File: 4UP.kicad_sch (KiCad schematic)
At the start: 34 parts, among them CON1 BARREL_JACK, J1 Conn_01x02_Male, J2 Conn_01x02_Male, J3 Conn_01x02_Male, P1 CONN_02X08, P2 CONN_02X08, SW1 SW_SPST, U1 VX078012-1000, U2 VX078012-1000, U3 VX078-500

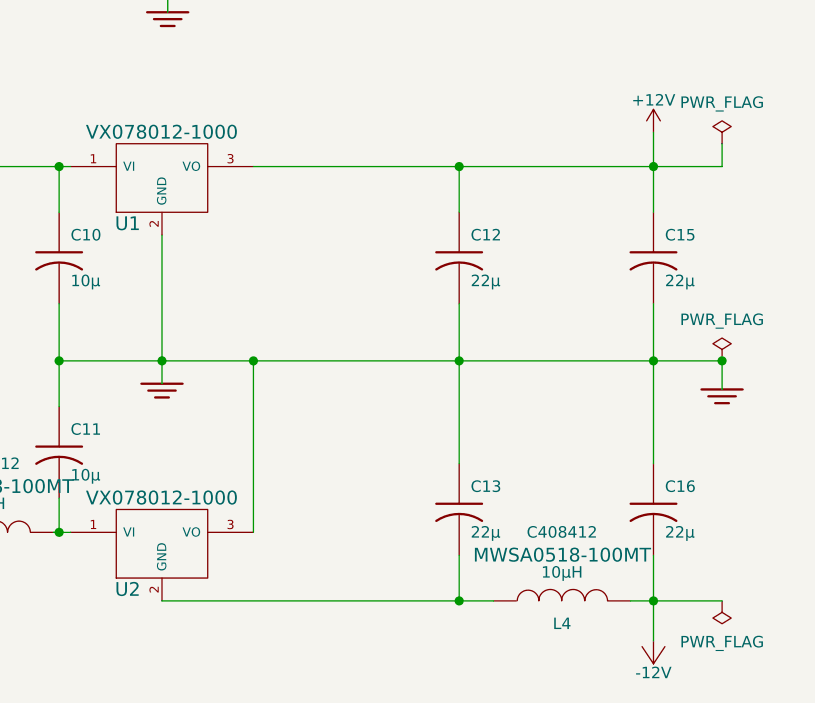
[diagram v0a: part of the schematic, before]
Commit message: fixed interference between bulk caps and VXO PSUs
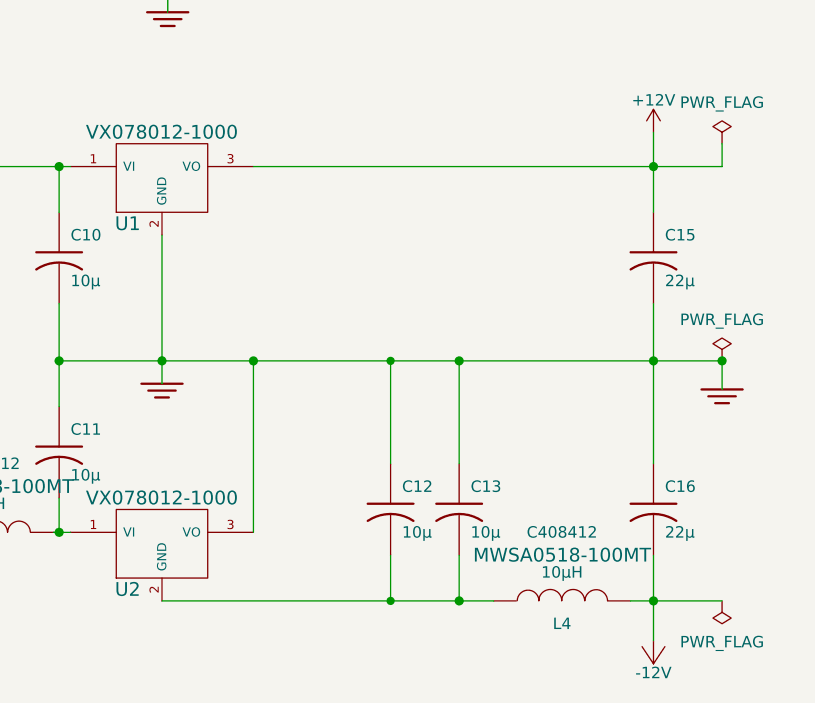
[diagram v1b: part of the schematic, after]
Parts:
- C12, C13: value 22µ -> 10µ; footprint Capacitor_SMD:C_1206_3216Metric -> Capacitor_SMD:C_0603_1608Metric; LCSC C12891 -> C96446
- L1, L2, L3, L4: footprint Inductor_SMD:L_Sunlord_MWSA0518_5.4x5.2mm -> MyFootprints:L_Sunlord_MWSA0518_5.4x5.2mm
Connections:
- net +12V: no longer C12.1
- net GND: now also C12.1; no longer C12.2
- net at C13.2, L4.1, U2.2 (GND): now also C12.2
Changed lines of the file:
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@@
   (junction (at 486.41 321.945) (diameter 1.016) (color 0 0 0 0)
   )
+  (junction (at 478.79 321.945) (diameter 0) (color 0 0 0 0)
+  )
   (junction (at 473.71 178.435) (diameter 0) (color 0 0 0 0)
   )
@@
   (junction (at 334.645 229.235) (diameter 1.016) (color 0 0 0 0)
   )
+  (junction (at 478.79 348.615) (diameter 0) (color 0 0 0 0)
+  )
   (junction (at 497.84 133.985) (diameter 1.016) (color 0 0 0 0)
   )
@@
   )
   (junction (at 453.39 321.945) (diameter 1.016) (color 0 0 0 0)
-  )
-  (junction (at 486.41 300.355) (diameter 1.016) (color 0 0 0 0)
   )
   (junction (at 515.62 321.945) (diameter 1.016) (color 0 0 0 0)
@@
     (stroke (width 0) (type solid) (color 0 0 0 0))
   )
-  (wire (pts (xy 453.39 348.615) (xy 486.41 348.615))
+  (wire (pts (xy 453.39 348.615) (xy 478.79 348.615))
     (stroke (width 0) (type solid) (color 0 0 0 0))
   )
@@
     (stroke (width 0) (type solid) (color 0 0 0 0))
   )
+  (wire (pts (xy 478.79 343.535) (xy 478.79 348.615))
+    (stroke (width 0) (type default) (color 0 0 0 0))
+  )
   (wire (pts (xy 487.045 280.035) (xy 487.045 278.765))
     (stroke (width 0) (type solid) (color 0 0 0 0))
@@
     (stroke (width 0) (type solid) (color 0 0 0 0))
   )
-  (wire (pts (xy 463.55 321.945) (xy 486.41 321.945))
+  (wire (pts (xy 463.55 321.945) (xy 478.79 321.945))
     (stroke (width 0) (type solid) (color 0 0 0 0))
   )
@@
     (stroke (width 0) (type solid) (color 0 0 0 0))
   )
-  (wire (pts (xy 486.41 315.595) (xy 486.41 321.945))
-    (stroke (width 0) (type solid) (color 0 0 0 0))
-  )
   (wire (pts (xy 486.41 321.945) (xy 486.41 333.375))
     (stroke (width 0) (type solid) (color 0 0 0 0))
@@
     (stroke (width 0) (type solid) (color 0 0 0 0))
   )
+  (wire (pts (xy 478.79 321.945) (xy 486.41 321.945))
+    (stroke (width 0) (type solid) (color 0 0 0 0))
+  )
   (wire (pts (xy 458.47 128.905) (xy 449.58 128.905))
     (stroke (width 0) (type solid) (color 0 0 0 0))
@@
   (wire (pts (xy 422.275 300.355) (xy 441.96 300.355))
     (stroke (width 0) (type solid) (color 0 0 0 0))
+  )
+  (wire (pts (xy 478.79 321.945) (xy 478.79 333.375))
+    (stroke (width 0) (type default) (color 0 0 0 0))
   )
   (wire (pts (xy 422.275 300.355) (xy 422.275 340.995))
@@
     (stroke (width 0) (type solid) (color 0 0 0 0))
   )
-  (wire (pts (xy 486.41 300.355) (xy 508 300.355))
+  (wire (pts (xy 463.55 300.355) (xy 508 300.355))
     (stroke (width 0) (type solid) (color 0 0 0 0))
   )
@@
     (stroke (width 0) (type solid) (color 0 0 0 0))
   )
+  (wire (pts (xy 478.79 348.615) (xy 486.41 348.615))
+    (stroke (width 0) (type solid) (color 0 0 0 0))
+  )
   (wire (pts (xy 400.685 265.43) (xy 400.685 300.355))
     (stroke (width 0) (type solid) (color 0 0 0 0))
@@
     (stroke (width 0) (type solid) (color 0 0 0 0))
   )
-  (wire (pts (xy 486.41 300.355) (xy 486.41 305.435))
-    (stroke (width 0) (type solid) (color 0 0 0 0))
-  )
   (wire (pts (xy 405.765 265.43) (xy 400.685 265.43))
     (stroke (width 0) (type solid) (color 0 0 0 0))
@@
     (stroke (width 0) (type solid) (color 0 0 0 0))
   )
-  (wire (pts (xy 463.55 300.355) (xy 486.41 300.355))
-    (stroke (width 0) (type solid) (color 0 0 0 0))
-  )
   (wire (pts (xy 340.36 236.22) (xy 340.36 229.235))
     (stroke (width 0) (type solid) (color 0 0 0 0))
@@
     (pin "~")
   )
-  (symbol (lib_id "VXO_PSU-rescue:C_US") (at 486.41 310.515 0) (unit 1)
-    (in_bom yes) (on_board yes)
-    (property "Reference" "C12" (id 0) (at 487.68 307.975 0)
-      (effects (font (size 1.27 1.27)) (justify left))
-    )
-    (property "Value" "22µ" (id 1) (at 487.68 313.055 0)
-      (effects (font (size 1.27 1.27)) (justify left))
-    )
-    (property "Footprint" "Capacitor_SMD:C_1206_3216Metric" (id 2) (at 486.41 310.515 0)
-      (effects (font (size 1.524 1.524)) hide)
-    )
-    (property "Datasheet" "" (id 3) (at 486.41 310.515 0)
-      (effects (font (size 1.524 1.524)))
-    )
-    (property "LCSC" "C12891" (id 4) (at 486.41 310.515 0)
-      (effects (font (size 1.27 1.27)) hide)
-    )
-    (pin "1")
-    (pin "2")
-  )
   (symbol (lib_id "VXO_PSU-rescue:C_US") (at 441.96 310.515 0) (unit 1)
     (in_bom yes) (on_board yes)
@@
     (property "Reference" "L1" (id 0) (at 412.75 302.895 90))
     (property "Value" "10µH" (id 1) (at 412.75 297.18 90))
-    (property "Footprint" "Inductor_SMD:L_Sunlord_MWSA0518_5.4x5.2mm" (id 2) (at 412.75 300.355 0)
+    (property "Footprint" "MyFootprints:L_Sunlord_MWSA0518_5.4x5.2mm" (id 2) (at 412.75 300.355 0)
       (effects (font (size 1.524 1.524)) hide)
     )
@@
       (effects (font (size 1.27 1.27)) (justify left))
     )
-    (property "Value" "22µ" (id 1) (at 487.68 340.995 0)
-      (effects (font (size 1.27 1.27)) (justify left))
-    )
-    (property "Footprint" "Capacitor_SMD:C_1206_3216Metric" (id 2) (at 486.41 338.455 0)
+    (property "Value" "10µ" (id 1) (at 487.68 340.995 0)
+      (effects (font (size 1.27 1.27)) (justify left))
+    )
+    (property "Footprint" "Capacitor_SMD:C_0603_1608Metric" (id 2) (at 486.41 338.455 0)
       (effects (font (size 1.524 1.524)) hide)
     )
@@
       (effects (font (size 1.524 1.524)))
     )
-    (property "LCSC" "C12891" (id 4) (at 486.41 338.455 0)
+    (property "LCSC" "C96446" (id 4) (at 486.41 338.455 0)
       (effects (font (size 1.27 1.27)) hide)
     )
@@
     (property "Reference" "L3" (id 0) (at 433.705 343.535 90))
     (property "Value" "10µH" (id 1) (at 433.705 337.82 90))
-    (property "Footprint" "Inductor_SMD:L_Sunlord_MWSA0518_5.4x5.2mm" (id 2) (at 433.705 340.995 0)
+    (property "Footprint" "MyFootprints:L_Sunlord_MWSA0518_5.4x5.2mm" (id 2) (at 433.705 340.995 0)
       (effects (font (size 1.524 1.524)) hide)
     )
@@
     (property "Reference" "L4" (id 0) (at 497.84 351.155 90))
     (property "Value" "10µH" (id 1) (at 497.84 345.44 90))
-    (property "Footprint" "Inductor_SMD:L_Sunlord_MWSA0518_5.4x5.2mm" (id 2) (at 497.84 348.615 0)
+    (property "Footprint" "MyFootprints:L_Sunlord_MWSA0518_5.4x5.2mm" (id 2) (at 497.84 348.615 0)
       (effects (font (size 1.524 1.524)) hide)
     )
@@
     )
     (pin "~")
+  )
+  (symbol (lib_id "VXO_PSU-rescue:C_US") (at 478.79 338.455 0) (unit 1)
+    (in_bom yes) (on_board yes)
+    (property "Reference" "C12" (id 0) (at 480.06 335.915 0)
+      (effects (font (size 1.27 1.27)) (justify left))
+    )
+    (property "Value" "10µ" (id 1) (at 480.06 340.995 0)
+      (effects (font (size 1.27 1.27)) (justify left))
+    )
+    (property "Footprint" "Capacitor_SMD:C_0603_1608Metric" (id 2) (at 478.79 338.455 0)
+      (effects (font (size 1.524 1.524)) hide)
+    )
+    (property "Datasheet" "" (id 3) (at 478.79 338.455 0)
+      (effects (font (size 1.524 1.524)))
+    )
+    (property "LCSC" "C96446" (id 4) (at 478.79 338.455 0)
+      (effects (font (size 1.27 1.27)) hide)
+    )
+    (pin "1")
+    (pin "2")
   )
   (symbol (lib_id "power1:+12V") (at 340.36 217.805 0) (unit 1)
@@
     (property "Reference" "L2" (id 0) (at 413.385 267.97 90))
     (property "Value" "10µH" (id 1) (at 413.385 262.255 90))
-    (property "Footprint" "Inductor_SMD:L_Sunlord_MWSA0518_5.4x5.2mm" (id 2) (at 413.385 265.43 0)
+    (property "Footprint" "MyFootprints:L_Sunlord_MWSA0518_5.4x5.2mm" (id 2) (at 413.385 265.43 0)
       (effects (font (size 1.524 1.524)) hide)
     )
@@
       (reference "C11") (unit 1) (value "10µ") (footprint "Capacitor_SMD:C_1206_3216Metric")
     )
-    (path "/00000000-0000-0000-0000-00005c480515"
-      (reference "C12") (unit 1) (value "22µ") (footprint "Capacitor_SMD:C_1206_3216Metric")
+    (path "/8dca1a50-0e75-490e-b512-fa5cf96dc6c4"
+      (reference "C12") (unit 1) (value "10µ") (footprint "Capacitor_SMD:C_0603_1608Metric")
     )
     (path "/00000000-0000-0000-0000-00005c4bf97a"
-      (reference "C13") (unit 1) (value "22µ") (footprint "Capacitor_SMD:C_1206_3216Metric")
+      (reference "C13") (unit 1) (value "10µ") (footprint "Capacitor_SMD:C_0603_1608Metric")
     )
     (path "/00000000-0000-0000-0000-00005d9b97e5"
@@
     )
     (path "/00000000-0000-0000-0000-00005c480569"
-      (reference "L1") (unit 1) (value "10µH") (footprint "Inductor_SMD:L_Sunlord_MWSA0518_5.4x5.2mm")
+      (reference "L1") (unit 1) (value "10µH") (footprint "MyFootprints:L_Sunlord_MWSA0518_5.4x5.2mm")
     )
     (path "/fff1db2b-1e63-4b1a-a271-5f15da541abd"
-      (reference "L2") (unit 1) (value "10µH") (footprint "Inductor_SMD:L_Sunlord_MWSA0518_5.4x5.2mm")
+      (reference "L2") (unit 1) (value "10µH") (footprint "MyFootprints:L_Sunlord_MWSA0518_5.4x5.2mm")
     )
     (path "/6383d9be-0754-4e78-b20d-99bb0b069c96"
-      (reference "L3") (unit 1) (value "10µH") (footprint "Inductor_SMD:L_Sunlord_MWSA0518_5.4x5.2mm")
+      (reference "L3") (unit 1) (value "10µH") (footprint "MyFootprints:L_Sunlord_MWSA0518_5.4x5.2mm")
     )
     (path "/697b9523-6938-475e-b51c-ef53a2c0769c"
-      (reference "L4") (unit 1) (value "10µH") (footprint "Inductor_SMD:L_Sunlord_MWSA0518_5.4x5.2mm")
+      (reference "L4") (unit 1) (value "10µH") (footprint "MyFootprints:L_Sunlord_MWSA0518_5.4x5.2mm")
     )
     (path "/00000000-0000-0000-0000-00005d9963e2"

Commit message: ready to order
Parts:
- C1, C4: LCSC Part Number (none) -> C15849
- C10, C11, C9: LCSC Part Number (none) -> C13585
- C12, C13: LCSC Part Number (none) -> C96446
- C14, C15, C16, C3, C6: LCSC Part Number (none) -> C12891
- C2, C5: LCSC Part Number (none) -> C1779
- C7: LCSC Part Number (none) -> C371974
- C8: LCSC Part Number (none) -> C132170
- D2: LCSC Part Number (none) -> C22452
- L1, L2, L3, L4: LCSC Part Number (none) -> C408412
- R1: LCSC Part Number (none) -> C22978
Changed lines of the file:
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@@
+      (effects (font (size 1.27 1.27)) hide)
+    )
+    (property "LCSC Part Number" "C13585" (id 5) (at 441.96 310.515 0)
       (effects (font (size 1.27 1.27)) hide)
     )
@@
     )
     (property "LCSC" "C408412" (id 5) (at 412.75 292.735 90))
+    (property "LCSC Part Number" "C408412" (id 6) (at 412.75 300.355 0)
+      (effects (font (size 1.27 1.27)) hide)
+    )
     (pin "1")
     (pin "2")
@@
       (effects (font (size 1.27 1.27)) hide)
     )
+    (property "LCSC Part Number" "C22452" (id 5) (at 387.985 300.355 0)
+      (effects (font (size 1.27 1.27)) hide)
+    )
     (pin "1")
     (pin "2")
@@
       (effects (font (size 1.27 1.27)) hide)
     )
+    (property "LCSC Part Number" "C12891" (id 5) (at 508 310.515 0)
+      (effects (font (size 1.27 1.27)) hide)
+    )
     (pin "1")
     (pin "2")
@@
       (effects (font (size 1.27 1.27)) hide)
     )
+    (property "LCSC Part Number" "C13585" (id 5) (at 441.96 332.105 0)
+      (effects (font (size 1.27 1.27)) hide)
+    )
     (pin "1")
     (pin "2")
@@
       (effects (font (size 1.27 1.27)) hide)
     )
+    (property "LCSC Part Number" "C96446" (id 5) (at 486.41 338.455 0)
+      (effects (font (size 1.27 1.27)) hide)
+    )
     (pin "1")
     (pin "2")
@@
       (effects (font (size 1.27 1.27)) hide)
     )
+    (property "LCSC Part Number" "C12891" (id 5) (at 508 338.455 0)
+      (effects (font (size 1.27 1.27)) hide)
+    )
     (pin "1")
     (pin "2")
@@
     )
     (property "LCSC" "C132170" (id 4) (at 400.685 309.88 0)
+      (effects (font (size 1.27 1.27)) hide)
+    )
+    (property "LCSC Part Number" "C132170" (id 5) (at 400.685 309.88 0)
       (effects (font (size 1.27 1.27)) hide)
     )
@@
       (effects (font (size 1.27 1.27)) hide)
     )
+    (property "LCSC Part Number" "C13585" (id 5) (at 441.96 274.955 0)
+      (effects (font (size 1.27 1.27)) hide)
+    )
     (pin "1")
     (pin "2")
@@
     )
     (property "LCSC" "C12891" (id 4) (at 487.045 273.685 0)
+      (effects (font (size 1.27 1.27)) hide)
+    )
+    (property "LCSC Part Number" "C12891" (id 5) (at 487.045 273.685 0)
       (effects (font (size 1.27 1.27)) hide)
     )
@@
     )
     (property "LCSC" "C371974" (id 4) (at 389.89 311.15 90))
+    (property "LCSC Part Number" "C371974" (id 5) (at 393.7 309.88 0)
+      (effects (font (size 1.27 1.27)) hide)
+    )
     (pin "1")
     (pin "2")
@@
       (effects (font (size 1.27 1.27)) hide)
     )
+    (property "LCSC Part Number" "C22978" (id 5) (at 354.33 335.915 0)
+      (effects (font (size 1.27 1.27)) hide)
+    )
     (pin "1")
     (pin "2")
@@
     )
     (property "LCSC" "C15849" (id 4) (at 272.415 224.155 0)
+      (effects (font (size 1.27 1.27)) hide)
+    )
+    (property "LCSC Part Number" "C15849" (id 5) (at 272.415 224.155 0)
       (effects (font (size 1.27 1.27)) hide)
     )
@@
       (effects (font (size 1.27 1.27)) hide)
     )
+    (property "LCSC Part Number" "C12891" (id 5) (at 334.645 224.155 0)
+      (effects (font (size 1.27 1.27)) hide)
+    )
     (pin "1")
     (pin "2")
@@
     )
     (property "LCSC" "C408412" (id 5) (at 433.705 333.375 90))
+    (property "LCSC Part Number" "C408412" (id 6) (at 433.705 340.995 0)
+      (effects (font (size 1.27 1.27)) hide)
+    )
     (pin "1")
     (pin "2")
@@
     )
     (property "LCSC" "C408412" (id 5) (at 497.84 340.995 90))
+    (property "LCSC Part Number" "C408412" (id 6) (at 497.84 348.615 0)
+      (effects (font (size 1.27 1.27)) hide)
+    )
     (pin "1")
     (pin "2")
@@
     )
     (property "LCSC" "C96446" (id 4) (at 478.79 338.455 0)
+      (effects (font (size 1.27 1.27)) hide)
+    )
+    (property "LCSC Part Number" "C96446" (id 5) (at 478.79 338.455 0)
       (effects (font (size 1.27 1.27)) hide)
     )
@@
     )
     (property "LCSC" "C1779" (id 4) (at 279.4 224.155 0)
+      (effects (font (size 1.27 1.27)) hide)
+    )
+    (property "LCSC Part Number" "C1779" (id 5) (at 279.4 224.155 0)
       (effects (font (size 1.27 1.27)) hide)
     )
@@
       (effects (font (size 1.27 1.27)) hide)
     )
+    (property "LCSC Part Number" "C12891" (id 5) (at 286.385 224.155 0)
+      (effects (font (size 1.27 1.27)) hide)
+    )
     (pin "1")
     (pin "2")
@@
       (effects (font (size 1.27 1.27)) hide)
     )
+    (property "LCSC Part Number" "C15849" (id 5) (at 320.675 224.155 0)
+      (effects (font (size 1.27 1.27)) hide)
+    )
     (pin "1")
     (pin "2")
@@
     )
     (property "LCSC" "C1779" (id 4) (at 327.66 224.155 0)
+      (effects (font (size 1.27 1.27)) hide)
+    )
+    (property "LCSC Part Number" "C1779" (id 5) (at 327.66 224.155 0)
       (effects (font (size 1.27 1.27)) hide)
     )
@@
     )
     (property "LCSC" "C408412" (id 5) (at 413.385 257.81 90))
-    (pin "1")
-    (pin "2")
+    (property "LCSC Part Number" "C408412" (id 6) (at 413.385 265.43 0)
+      (effects (font (size 1.27 1.27)) hide)
+    )
+    (pin "1")
+    (pin "2")
